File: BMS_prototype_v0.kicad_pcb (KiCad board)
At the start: 2 copper layers, 124.8 x 94.7 mm, 119 parts, among them J1 Conn_02x12_Odd_Even, J2 Conn_01x13_Pin, J3 Conn_01x02_Pin, J4 Conn_01x02_Pin, J5 Conn_02x08_Odd_Even, J7 Conn_01x03_Pin, Q2 Q_NMOS_GSD, Q3 Q_NMOS_GSD, Q4 Q_NMOS_GSD, Q5 Q_NMOS_GSD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

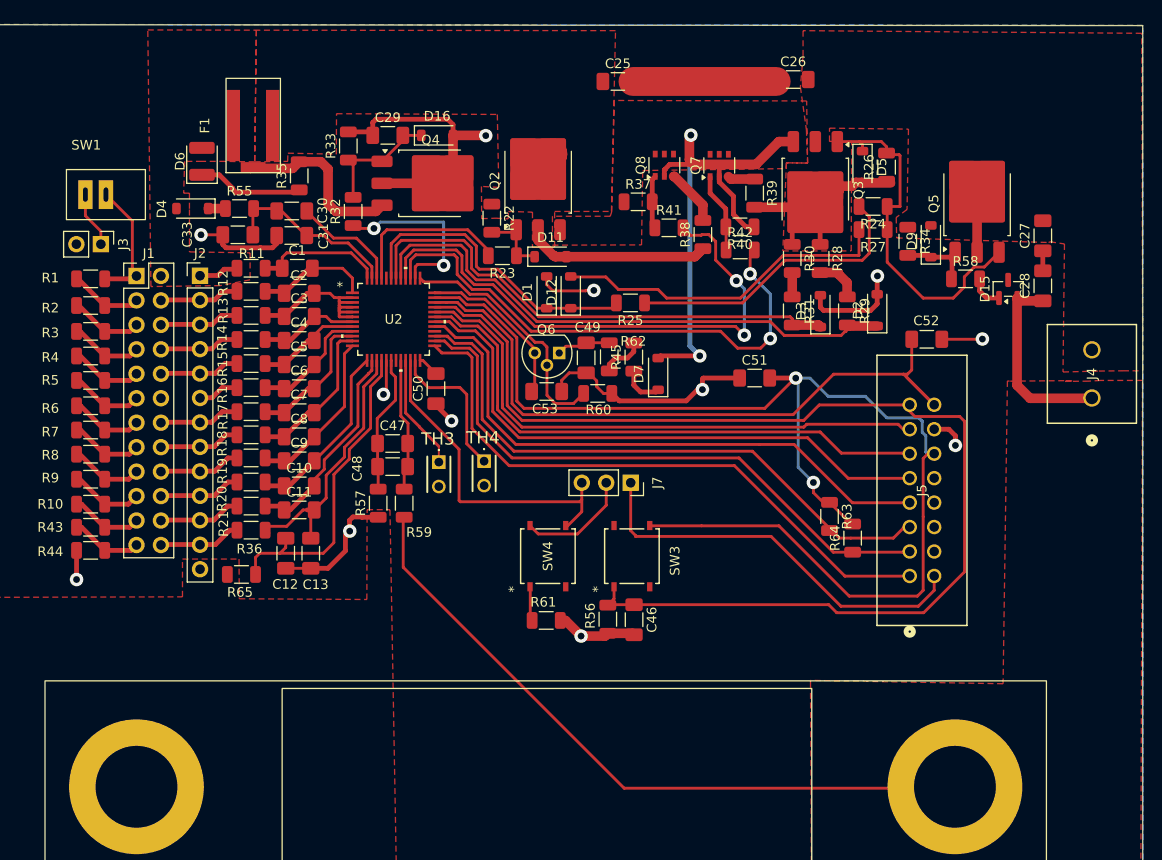
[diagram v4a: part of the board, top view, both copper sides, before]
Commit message: posiciona testpoints
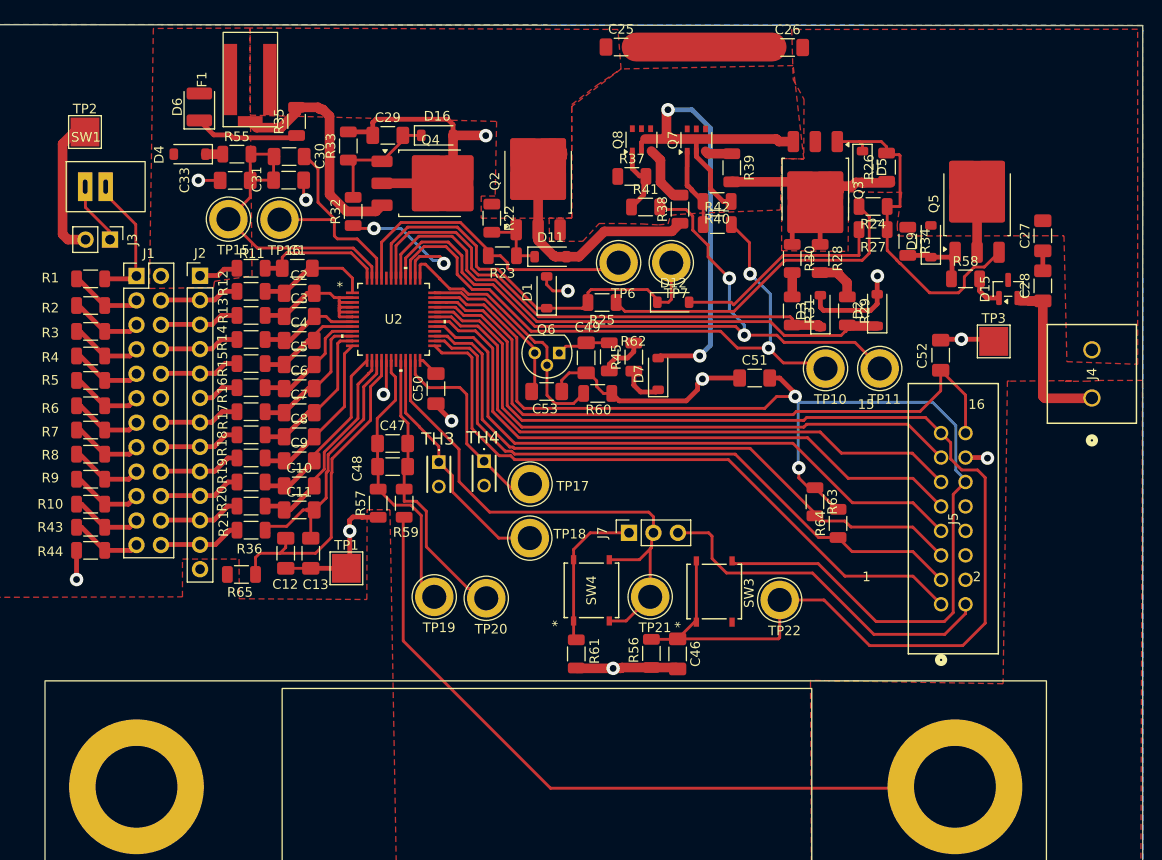
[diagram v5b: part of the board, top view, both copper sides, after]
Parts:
- added TP1: TestPoint, TestPoint:TestPoint_Pad_3.0x3.0mm, F.Cu at (120.8, 113.1)
- added TP10: TestPoint, TestPoint:TestPoint_Loop_D3.80mm_Drill2.5mm, F.Cu at (170.6, 92.3)
- added TP11: TestPoint, TestPoint:TestPoint_Loop_D3.80mm_Drill2.5mm, F.Cu at (176.2, 92.3)
- added TP15: TestPoint, TestPoint:TestPoint_Loop_D3.80mm_Drill2.5mm, F.Cu at (108.5, 76.8)
- added TP16: TestPoint, TestPoint:TestPoint_Loop_D3.80mm_Drill2.5mm, F.Cu at (113.8, 76.8)
- added TP17: TestPoint, TestPoint:TestPoint_Loop_D3.80mm_Drill2.5mm, F.Cu at (139.9, 104.3)
- added TP18: TestPoint, TestPoint:TestPoint_Loop_D3.80mm_Drill2.5mm, F.Cu at (139.8, 109.9)
- added TP19: TestPoint, TestPoint:TestPoint_Loop_D3.80mm_Drill2.5mm, F.Cu at (129.9, 116.0)
- added TP2: TestPoint, TestPoint:TestPoint_Pad_3.0x3.0mm, F.Cu at (93.7, 67.8)
- added TP20: TestPoint, TestPoint:TestPoint_Loop_D3.80mm_Drill2.5mm, F.Cu at (135.3, 116.2)
- added TP21: TestPoint, TestPoint:TestPoint_Loop_D3.80mm_Drill2.5mm, F.Cu at (152.3, 116.0)
- added TP22: TestPoint, TestPoint:TestPoint_Loop_D3.80mm_Drill2.5mm, F.Cu at (165.8, 116.3)
- added TP3: TestPoint, TestPoint:TestPoint_Pad_3.0x3.0mm, F.Cu at (188.0, 89.5)
- added TP6: TestPoint, TestPoint:TestPoint_Loop_D3.80mm_Drill2.5mm, F.Cu at (149.1, 81.3)
- added TP7: TestPoint, TestPoint:TestPoint_Loop_D3.80mm_Drill2.5mm, F.Cu at (154.5, 81.3)
- moved D12 10.7 mm to (154.7, 85.4), turned to 0 degrees
- moved SW3 9.31 mm to (159.0, 115.5)
- moved C31 5.76 mm to (114.8, 72.8), turned to 0 degrees
- moved R56 5.75 mm to (152.5, 121.9)
- moved SW4 5.75 mm to (146.2, 115.3)
- moved C46 5.75 mm to (155.2, 122.0)
- moved C30 5.66 mm to (114.8, 70.3)
- moved D4 5.66 mm to (104.5, 70.0)
- moved D6 5.66 mm to (105.5, 65.1)
- moved R55 5.66 mm to (109.4, 70.0)
- moved C33 5.66 mm to (109.2, 72.8)
- moved R35 5.66 mm to (115.6, 66.7)
- moved J7 5.20 mm to (150.2, 109.4), turned to 90 degrees
- moved F1 4.78 mm to (110.8, 62.3)
- moved R61 4.67 mm to (144.7, 122.0), turned to 90 degrees
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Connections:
- J7 pad 1: EXTTS2 -> Net-(J7-Pin_1)
- J7 pad 3: Net-(J7-Pin_3) -> EXTTS2
- R61 pad 2: Net-(J7-Pin_2) -> Net-(J7-Pin_1)
- SW4 pad 1: Net-(J7-Pin_2) -> Net-(J7-Pin_1)
- SW4 pad 2: Net-(J7-Pin_2) -> Net-(J7-Pin_1)
- SW4 pad 3: Net-(J7-Pin_3) -> Net-(J7-Pin_2)
- SW4 pad 4: Net-(J7-Pin_3) -> Net-(J7-Pin_2)
- U2 pad 22: Net-(J7-Pin_3) -> Net-(J7-Pin_2)
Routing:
- net Net-(J7-Pin_2): track 15.3 -> 55.2 mm
- net Net-(J7-Pin_3): track 34.8 -> 0.00 mm
- net PCHG: track 58.1 -> 78.0 mm
- net /Folha de monitoramento BMS/SRN: track 13.6 -> 30.5 mm
- net CHG: track 17.2 -> 33.7 mm
- net Net-(J7-Pin_1): track 0.00 -> 16.0 mm
- net BAT: track 19.1 -> 33.8 mm
- net /Folha de monitoramento BMS/SRP: track 14.4 -> 29.0 mm
- net DSG : track 31.2 -> 45.2 mm
- net Net-(U2-TS1): track 12.0 -> 25.7 mm
- net RST_SHUT: track 122.1 -> 135.4 mm
- net Net-(D12-A): track 35.4 -> 22.6 mm
- net CP1: track 11.8 -> 23.3 mm
- net PDSG: track 54.2 -> 65.0 mm
- net CD: track 54.7 -> 65.4 mm
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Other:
- board text added: "1"
- board text added: "15"
- board text added: "16"
- board text added: "2"

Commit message: salva 12/02
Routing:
- net 7P: track 4.15 -> 8.22 mm
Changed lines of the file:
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@@
 	)
 	(segment
+		(start 105.575 95.4)
+		(end 105.6 95.375)
+		(width 0.3)
+		(layer "F.Cu")
+		(net 55)
+	)
+	(segment
 		(start 107.9 94.3)
 		(end 109.4375 94.3)
@@
 	)
 	(segment
+		(start 101.54 95.4)
+		(end 105.575 95.4)
+		(width 0.3)
+		(layer "F.Cu")
+		(net 55)
+	)
+	(segment
 		(start 148.1292 112.21865)
 		(end 148.28635 112.21865)
@@
 			(pts
 				(xy 166 80.075) (xy 172.9 80.15) (xy 172.975 73.95) (xy 176.9 74.025) (xy 178.475 74) (xy 178 77.4)
-				(xy 178.075 78.55) (xy 193.125 78.525) (xy 195.325 78.525) (xy 195.625 91.6) (xy 202.975 91.875)
+				(xy 178.075 78.55) (xy 193.125 78.525) (xy 195.325 78.525) (xy 195.45 93.65) (xy 203.05 93.625)
 				(xy 202.975 57.075) (xy 167.05 57.1) (xy 167.2 62.3) (xy 168.325 64.35) (xy 168.3 70.55) (xy 166 70.5)
-				(xy 166 80.075) (xy 166 80.075) (xy 166 80.075)
 			)
 		)
